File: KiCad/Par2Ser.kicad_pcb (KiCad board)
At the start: 4 copper layers, 47 x 50 mm, 41 parts, among them J1 DB25_Male, J2 USB_C_Receptacle_USB2.0, J3 Conn_02x05_Odd_Even, U1 LC4064V-75TN48C, U2 FT240XS-R, U3 TLV75533PDBVR

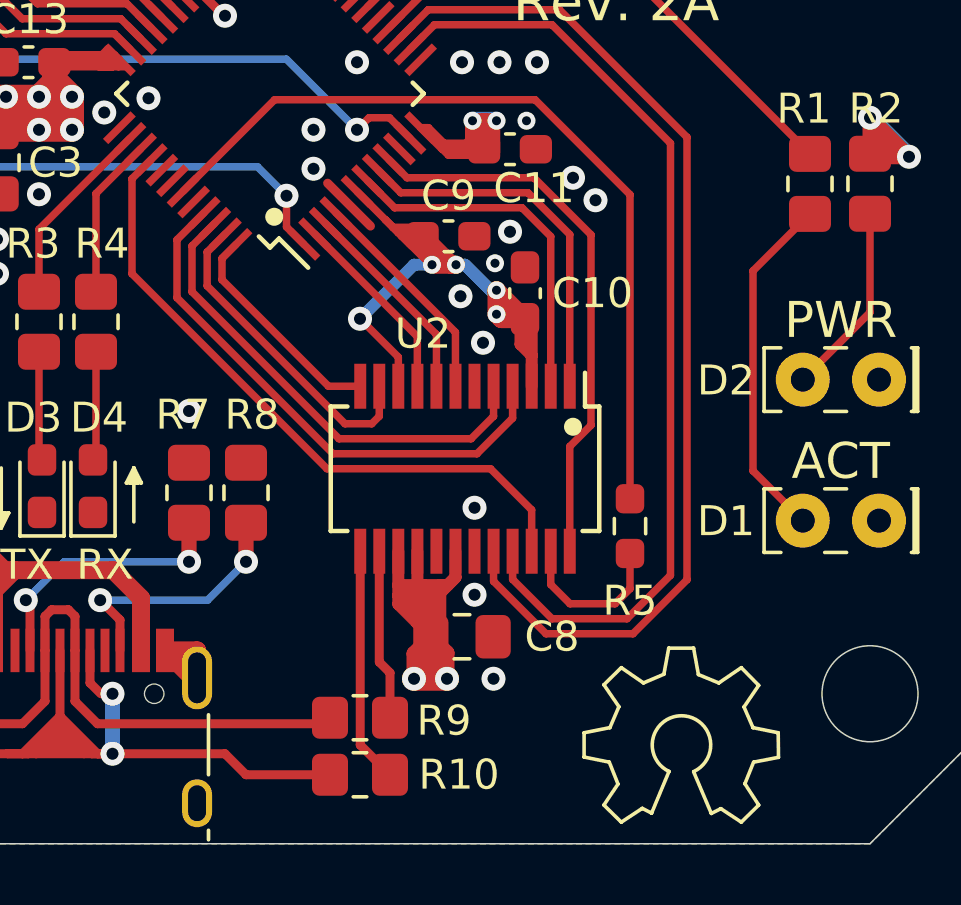
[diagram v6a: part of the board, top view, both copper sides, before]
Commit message: Change Ohm values on R1 (1k for Yellow ACT LED) and R2 (10k for Power indicator LED) tested and verified suitable levels of glow
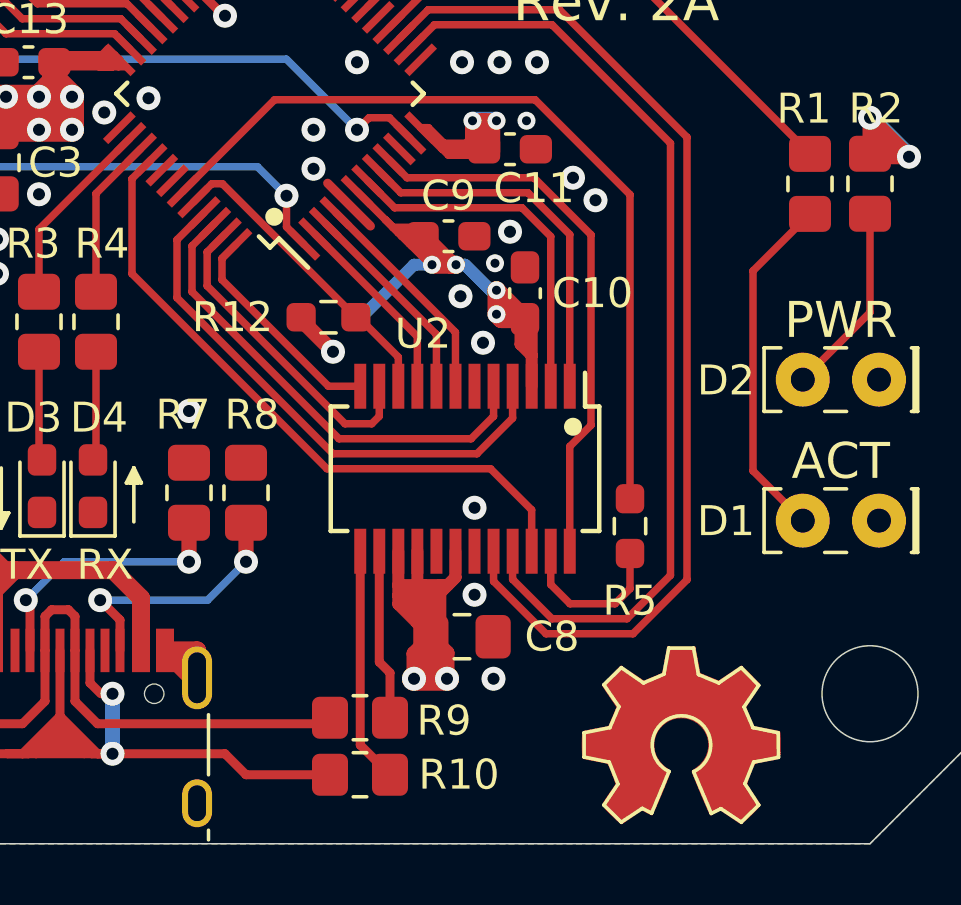
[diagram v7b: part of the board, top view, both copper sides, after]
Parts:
- added R12: 10k, Resistor_SMD:R_0603_1608Metric_Pad0.98x0.95mm_HandSolder, F.Cu at (149.4, 117.5)
- added REF**: OSHW-Symbol_6.7x6mm_Copper, Symbol:OSHW-Symbol_6.7x6mm_Copper, F.Cu at (161.2, 131.4)
- R1: value 330 -> 1k
- R2: value 330 -> 10k
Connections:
- U1 pad 44: Net-(U1-Pad44) -> SIWU
- U2 pad 10: 3V3 -> SIWU
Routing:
- net SIWU: track 0.00 -> 10.3 mm
- net 3V3: track 134.3 -> 133.1 mm

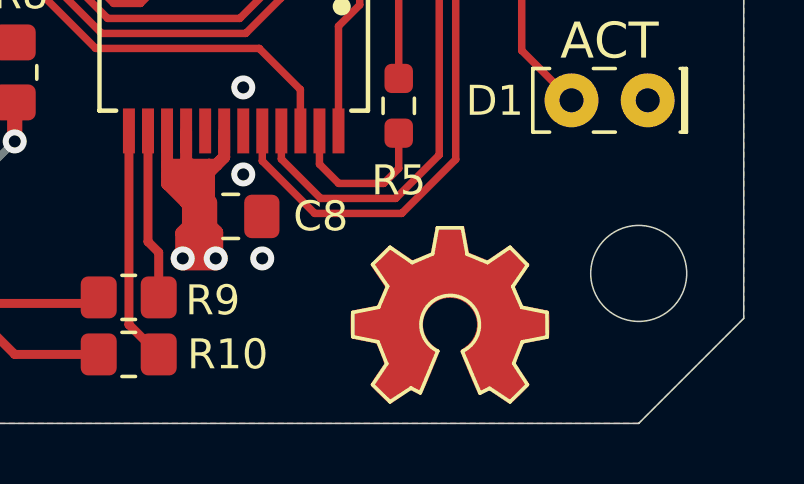
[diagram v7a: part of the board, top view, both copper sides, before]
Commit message: Cosmetic fix remove OSHW copper symbol leaving cog wheel area unfilled
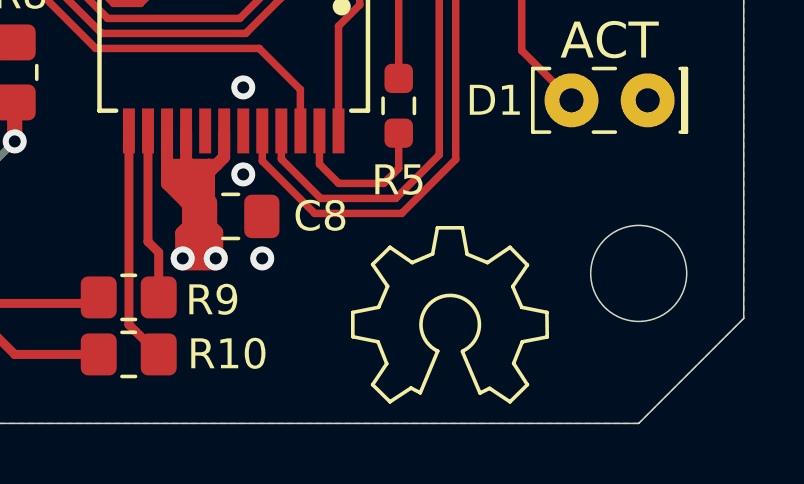
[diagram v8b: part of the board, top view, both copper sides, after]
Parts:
- removed the REF** at (161.2, 131.4)
